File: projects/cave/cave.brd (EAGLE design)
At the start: 100 x 72 mm, 111 parts, among them U1 IRLML6344TRPBF, U10 IRLML6344TRPBF, U11 IRLML6344TRPBF, U12 IRLML6344TRPBF, U2 TLC555CDR, U3 IRLML6344TRPBF, U4 IRLML6344TRPBF, U5 IRLML6344TRPBF, U6 IRLML6344TRPBF, U7 TPS54625, U9 IRLML6344TRPBF

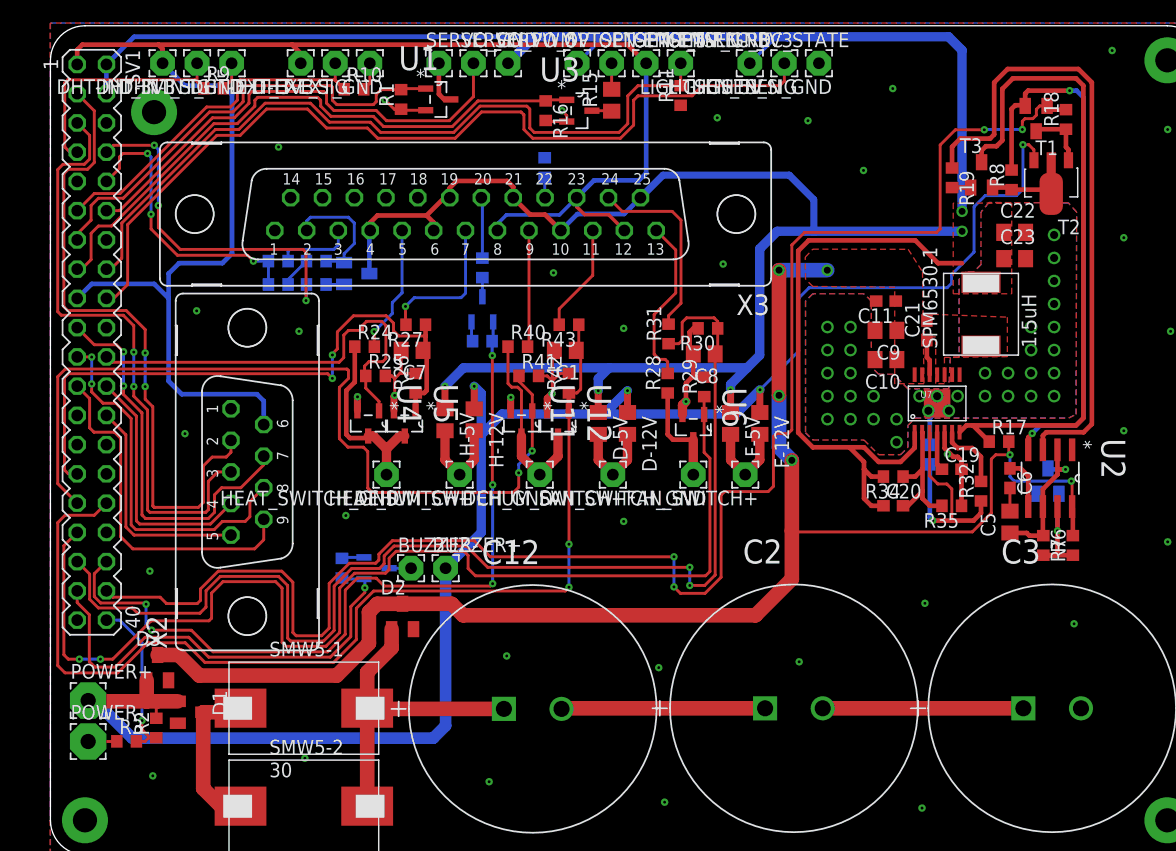
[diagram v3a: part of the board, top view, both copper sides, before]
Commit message: Added silkscreen on board (_tsilk layer). Changed GND pin name in STM library (moved to personnal lib).
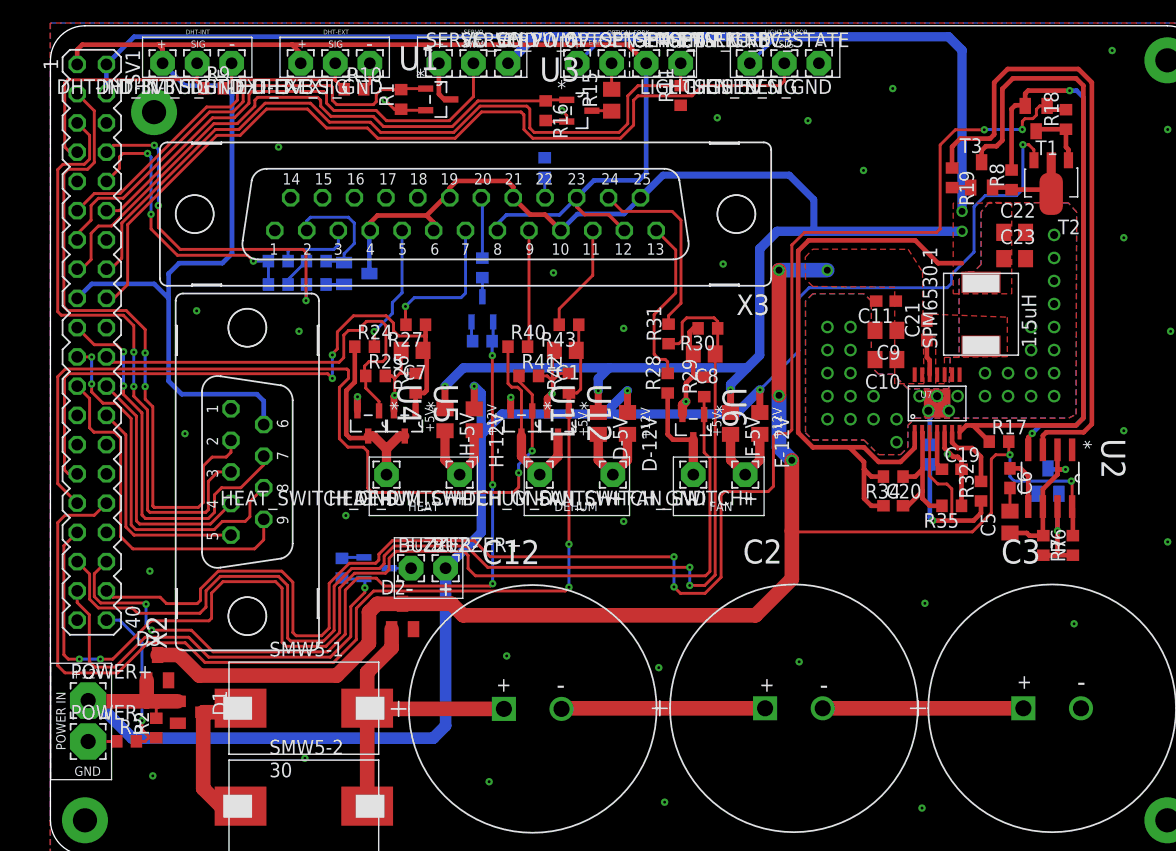
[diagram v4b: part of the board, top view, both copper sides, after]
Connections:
- net GND: now also U2.1-GND; no longer U2.1
- net N$12: now also U2.4-RESET; no longer U2.4
- net N$16: now also U2.3-OUT; no longer U2.3
- net N$5: now also U2.7-DIS; no longer U2.7
- net N$6: now also U2.2-TRIG, U2.6-THR; no longer U2.2, U2.6
- net N$9: now also U2.5-CONT; no longer U2.5
- net VCOND: now also U2.8-VDD; no longer U2.8
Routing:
- net GND: vias 73 -> 77
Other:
- board text added: "+"
- board text added: "+12V"
- board text added: "+5V"
- board text added: "-"
- board text added: "BUZZER"
- board text added: "DEHUM"
- board text added: "DHT-EXT"
- board text added: "DHT-INT"
- board text added: "EMIT"
- board text added: "FAN"
- board text added: "GND"
- board text added: "HEAT"
- board text added: "LIGHT SENSOR"
- board text added: "OPTICAL FORK"
- board text added: "POWER IN"
- board text added: "PWM"
- board text added: "REC"
- board text added: "SERVO"
- board text added: "SIG"
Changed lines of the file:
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@@
 <setting verticaltext="up"/>
 </settings>
-<grid distance="0.5" unitdist="mm" unit="mm" style="lines" multiple="1" display="yes" altdistance="10" altunitdist="mil" altunit="mil"/>
+<grid distance="1" unitdist="mil" unit="mm" style="lines" multiple="1" display="yes" altdistance="10" altunitdist="mil" altunit="mil"/>
 <layers>
 <layer number="1" name="Top" color="4" fill="1" visible="yes" active="yes"/>
@@
 <wire x1="97" y1="72" x2="3" y2="72" width="0" layer="20"/>
 <wire x1="3" y1="72" x2="0" y2="69" width="0" layer="20" curve="90"/>
+<text x="11.754" y="71.254" size="0.4064" layer="121">DHT-INT</text>
+<wire x1="8" y1="71.008" x2="17.5" y2="71.008" width="0.1" layer="121"/>
+<wire x1="17.5" y1="71.008" x2="17.5" y2="67.524" width="0.1" layer="121"/>
+<wire x1="17.5" y1="67.524" x2="8" y2="67.524" width="0.1" layer="121"/>
+<wire x1="8" y1="67.524" x2="8" y2="71.008" width="0.1" layer="121"/>
+<text x="9.246" y="70.048" size="0.8128" layer="121">+</text>
+<text x="12.192" y="70.104" size="0.6096" layer="121">SIG</text>
+<text x="15.494" y="69.85" size="1.27" layer="121">-</text>
+<text x="23.692" y="71.254" size="0.4064" layer="121">DHT-EXT</text>
+<wire x1="19.938" y1="71.008" x2="29.438" y2="71.008" width="0.1" layer="121"/>
+<wire x1="29.438" y1="71.008" x2="29.438" y2="67.524" width="0.1" layer="121"/>
+<wire x1="29.438" y1="67.524" x2="19.938" y2="67.524" width="0.1" layer="121"/>
+<wire x1="19.938" y1="67.524" x2="19.938" y2="71.008" width="0.1" layer="121"/>
+<text x="21.438" y="70.048" size="0.8128" layer="121">+</text>
+<text x="24.13" y="70.104" size="0.6096" layer="121">SIG</text>
+<text x="27.432" y="69.85" size="1.27" layer="121">-</text>
+<text x="35.884" y="71.254" size="0.4064" layer="121">SERVO</text>
+<wire x1="31.876" y1="71.008" x2="41.376" y2="71.008" width="0.1" layer="121"/>
+<wire x1="41.376" y1="71.008" x2="41.376" y2="67.524" width="0.1" layer="121"/>
+<wire x1="41.376" y1="67.524" x2="31.876" y2="67.524" width="0.1" layer="121"/>
+<wire x1="31.876" y1="67.524" x2="31.876" y2="71.008" width="0.1" layer="121"/>
+<text x="33.376" y="70.048" size="0.8128" layer="121">+</text>
+<text x="35.814" y="70.104" size="0.6096" layer="121">PWM</text>
+<text x="39.37" y="69.85" size="1.27" layer="121">-</text>
+<text x="62.046" y="71.254" size="0.4064" layer="121">LIGHT SENSOR</text>
+<wire x1="59.054" y1="71.008" x2="68.554" y2="71.008" width="0.1" layer="121"/>
+<wire x1="68.554" y1="71.008" x2="68.554" y2="67.524" width="0.1" layer="121"/>
+<wire x1="68.554" y1="67.524" x2="59.054" y2="67.524" width="0.1" layer="121"/>
+<wire x1="59.054" y1="67.524" x2="59.054" y2="71.008" width="0.1" layer="121"/>
+<text x="60.3" y="70.048" size="0.8128" layer="121">+</text>
+<text x="63.246" y="70.104" size="0.6096" layer="121">SIG</text>
+<text x="66.548" y="69.85" size="1.27" layer="121">-</text>
+<text x="48.3554" y="71.2032" size="0.4064" layer="121">OPTICAL FORK</text>
+<wire x1="44.322" y1="71.008" x2="56.108" y2="71.008" width="0.1" layer="121"/>
+<wire x1="56.108" y1="71.008" x2="56.108" y2="67.524" width="0.1" layer="121"/>
+<wire x1="56.108" y1="67.524" x2="44.322" y2="67.524" width="0.1" layer="121"/>
+<wire x1="44.322" y1="67.524" x2="44.322" y2="71.008" width="0.1" layer="121"/>
+<text x="45.314" y="70.048" size="0.8128" layer="121">+</text>
+<text x="48.514" y="69.85" size="1.27" layer="121">-</text>
+<text x="51.308" y="70.104" size="0.8128" layer="121">+</text>
+<text x="54.356" y="70.104" size="0.6096" layer="121">SIG</text>
+<wire x1="50.292" y1="67.564" x2="50.292" y2="70.866" width="0.1" layer="121" style="shortdash"/>
+<text x="46.736" y="70.358" size="0.4064" layer="121">EMIT</text>
+<text x="52.578" y="70.358" size="0.4064" layer="121">REC</text>
+<wire x1="27.686" y1="34.544" x2="37.084" y2="34.544" width="0.1" layer="121"/>
+<wire x1="37.084" y1="34.544" x2="37.084" y2="29.464" width="0.1" layer="121"/>
+<wire x1="37.084" y1="29.464" x2="27.686" y2="29.464" width="0.1" layer="121"/>
+<wire x1="27.686" y1="29.464" x2="27.686" y2="34.544" width="0.1" layer="121"/>
+<text x="31.058" y="29.852" size="0.8128" layer="121">HEAT</text>
+<text x="34.9" y="30.424" size="1.27" layer="121">+</text>
+<text x="28.702" y="30.226" size="1.6764" layer="121">-</text>
+<wire x1="41.148" y1="34.544" x2="50.292" y2="34.544" width="0.1" layer="121"/>
+<wire x1="50.292" y1="34.544" x2="50.292" y2="29.464" width="0.1" layer="121"/>
+<wire x1="50.292" y1="29.464" x2="41.148" y2="29.464" width="0.1" layer="121"/>
+<wire x1="41.148" y1="29.464" x2="41.148" y2="34.544" width="0.1" layer="121"/>
+<text x="43.758" y="29.852" size="0.8128" layer="121">DEHUM</text>
+<text x="48.362" y="30.424" size="1.27" layer="121">+</text>
+<text x="42.164" y="30.226" size="1.6764" layer="121">-</text>
+<wire x1="54.102" y1="34.544" x2="61.976" y2="34.544" width="0.1" layer="121"/>
+<wire x1="61.976" y1="34.544" x2="61.976" y2="29.464" width="0.1" layer="121"/>
+<wire x1="61.976" y1="29.464" x2="54.102" y2="29.464" width="0.1" layer="121"/>
+<wire x1="54.102" y1="29.464" x2="54.102" y2="34.544" width="0.1" layer="121"/>
+<text x="57.22" y="29.852" size="0.8128" layer="121">FAN</text>
+<text x="59.792" y="30.424" size="1.27" layer="121">+</text>
+<text x="55.372" y="30.226" size="1.6764" layer="121">-</text>
+<text x="33.3248" y="36.6776" size="0.8128" layer="121" rot="R90">+5V</text>
+<text x="38.735" y="36.3474" size="0.8128" layer="121" rot="R90">+12V</text>
+<text x="52.07" y="36.068" size="0.8128" layer="121" rot="R90">+12V</text>
+<text x="63.5" y="36.068" size="0.8128" layer="121" rot="R90">+12V</text>
+<text x="58.2676" y="36.2966" size="0.8128" layer="121" rot="R90">+5V</text>
+<text x="46.6344" y="36.322" size="0.8128" layer="121" rot="R90">+5V</text>
+<text x="83.922" y="14.422" size="1.27" layer="121">+</text>
+<text x="89.154" y="14.224" size="1.6764" layer="121">-</text>
+<text x="61.57" y="14.168" size="1.27" layer="121">+</text>
+<text x="66.802" y="13.97" size="1.6764" layer="121">-</text>
+<text x="38.71" y="14.168" size="1.27" layer="121">+</text>
+<text x="43.942" y="13.97" size="1.6764" layer="121">-</text>
+<text x="30.931" y="26.423" size="0.8128" layer="121">BUZZER</text>
+<text x="30.8102" y="22.3774" size="1.6764" layer="121">-</text>
+<text x="33.6808" y="22.4992" size="1.27" layer="121">+</text>
+<text x="33.6554" y="22.4992" size="1.27" layer="121">+</text>
+<wire x1="29.8704" y1="27.5336" x2="35.814" y2="27.5336" width="0.1" layer="121"/>
+<wire x1="35.814" y1="27.5336" x2="35.814" y2="22.2758" width="0.1" layer="121"/>
+<wire x1="35.814" y1="22.2758" x2="29.8704" y2="22.2758" width="0.1" layer="121"/>
+<wire x1="29.8704" y1="22.2758" x2="29.8704" y2="27.5336" width="0.1" layer="121"/>
+<text x="1.3138" y="9.087" size="0.8128" layer="121" rot="R90">POWER IN</text>
+<text x="1.8288" y="15.3162" size="0.8128" layer="121">+12V</text>
+<text x="2.0828" y="6.858" size="0.8128" layer="121">GND</text>
+<wire x1="0.0254" y1="16.637" x2="5.3086" y2="16.637" width="0.1" layer="121"/>
+<wire x1="5.3086" y1="16.637" x2="5.3086" y2="6.5278" width="0.1" layer="121"/>
+<wire x1="5.3086" y1="6.5278" x2="0.0254" y2="6.5278" width="0.1" layer="121"/>
+<wire x1="0.0254" y1="6.5278" x2="0.0254" y2="16.637" width="0.1" layer="121"/>
 </plain>
 <attributes>
@@
 <contactref element="SV1" pad="30"/>
 <contactref element="SV1" pad="34"/>
-<contactref element="U2" pad="1"/>
+<contactref element="U2" pad="1-GND"/>
 <contactref element="C6" pad="2"/>
 <contactref element="R8" pad="1"/>
@@
 <via x="21.59" y="45.466" extent="1-16" drill="0.25"/>
 <via x="8.636" y="24.638" extent="1-16" drill="0.25"/>
+<via x="97" y="69" extent="1-16" drill="2.1" diameter="4"/>
+<via x="97" y="3" extent="1-16" drill="2.1" diameter="4"/>
+<via x="3" y="3" extent="1-16" drill="2.1" diameter="4"/>
+<via x="9" y="64.5" extent="1-16" drill="2.1" diameter="4"/>
 </signal>
 <signal name="DHT22_EXT">
@@
 </signal>
 <signal name="VCOND">
-<contactref element="U2" pad="8"/>
+<contactref element="U2" pad="8-VDD"/>
 <contactref element="R6" pad="2"/>
 <contactref element="R17" pad="2"/>
@@
 </signal>
 <signal name="N$5">
-<contactref element="U2" pad="7"/>
+<contactref element="U2" pad="7-DIS"/>
 <contactref element="R7" pad="2"/>
 <contactref element="R6" pad="1"/>
@@
 </signal>
 <signal name="N$6">
-<contactref element="U2" pad="2"/>
-<contactref element="U2" pad="6"/>
+<contactref element="U2" pad="2-TRIG"/>
+<contactref element="U2" pad="6-THR"/>
 <contactref element="R7" pad="1"/>
 <contactref element="C5" pad="1"/>
@@
 <signal name="N$9">
 <contactref element="C6" pad="1"/>
-<contactref element="U2" pad="5"/>
+<contactref element="U2" pad="5-CONT"/>
 <wire x1="84.9177" y1="30.2472" x2="84.9177" y2="32.9015" width="0.4064" layer="1"/>
 <wire x1="84.9177" y1="32.9015" x2="84.2582" y2="33.561" width="0.4064" layer="1"/>
@@
 <signal name="N$12">
 <contactref element="R8" pad="2"/>
-<contactref element="U2" pad="4"/>
+<contactref element="U2" pad="4-RESET"/>
 <contactref element="T1" pad="E"/>
 <wire x1="89.0706" y1="37.2957" x2="89.7056" y2="37.9307" width="0.4064" layer="16"/>
@@
 </signal>
 <signal name="N$16">
-<contactref element="U2" pad="3"/>
+<contactref element="U2" pad="3-OUT"/>
 <contactref element="R19" pad="1"/>
 <wire x1="89.731" y1="36.6988" x2="90.4422" y2="37.41" width="0.4064" layer="1"/>
@@
 <signal name="N$39">
 </signal>
-<signal name="N$8">
-<via x="3" y="3" extent="1-16" drill="2.1" diameter="4"/>
-</signal>
-<signal name="N$18">
-<via x="97" y="3" extent="1-16" drill="2.1" diameter="4"/>
-</signal>
-<signal name="N$19">
-<via x="97" y="69" extent="1-16" drill="2.1" diameter="4"/>
-</signal>
-<signal name="N$29">
-<via x="9" y="64.5" extent="1-16" drill="2.1" diameter="4"/>
-</signal>
 </signals>

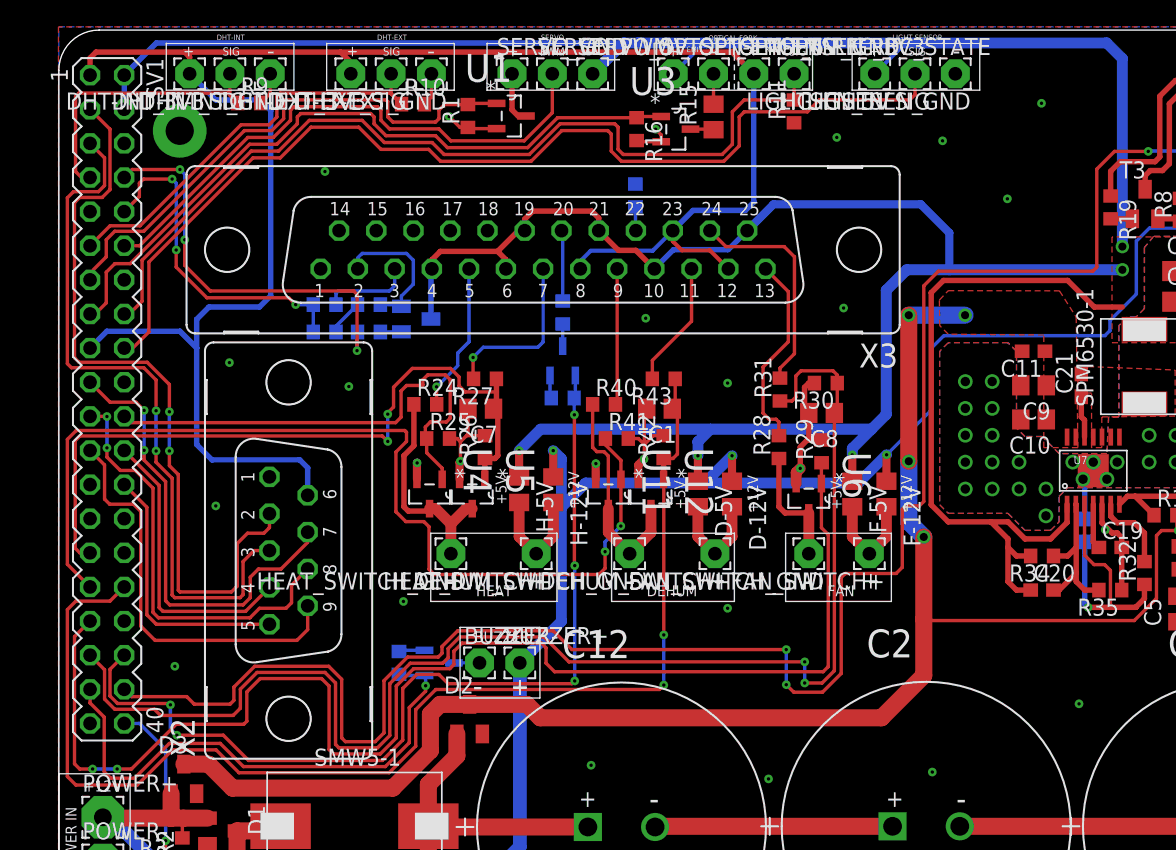
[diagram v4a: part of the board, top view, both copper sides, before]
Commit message: Silkscreen moved to tDocu layer. Added some space between the MOSFET. Modified 40-pin-header package's silkscreen and saved it to HE_254.lbr.
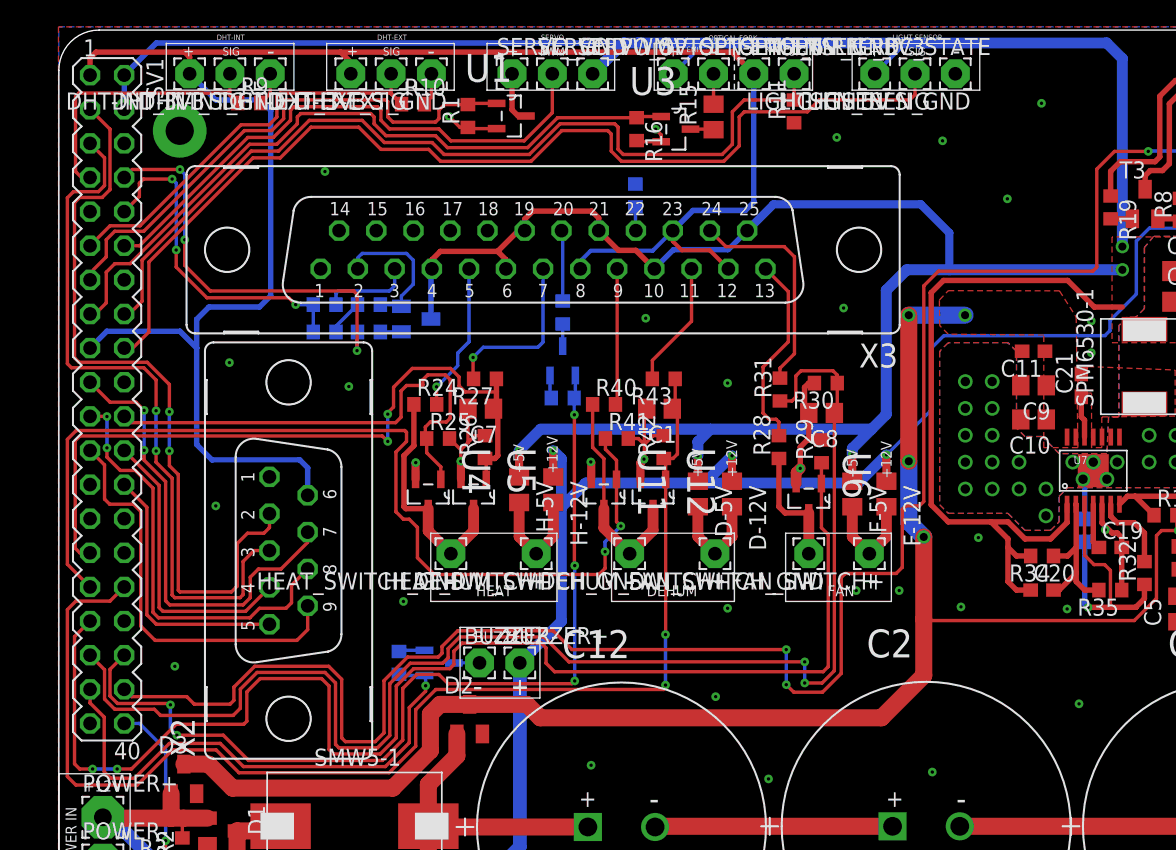
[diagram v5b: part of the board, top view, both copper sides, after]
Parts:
- SV1: device con-lstb:MA20-2 -> HE_254:MA20-2
- moved U11 0.33 mm to (40.6, 37.5)
- moved U12 0.15 mm to (44.2, 37.5)
- moved U4 0.10 mm to (27.5, 37.5)
- moved U5 0.10 mm to (30.9, 37.5)
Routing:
- net N$21: track 16.4 -> 17.9 mm
- net DEHUM_SWITCH: track 73.7 -> 73.2 mm
- net GND: track 66.9 -> 67.3 mm, vias 77 -> 85
